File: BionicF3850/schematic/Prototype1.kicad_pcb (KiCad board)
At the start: 2 copper layers, 48.3 x 71.1 mm, 11 parts, among them J1 BionicConnector, U1 F3850, U2 74HCT126, U3 LM78L12

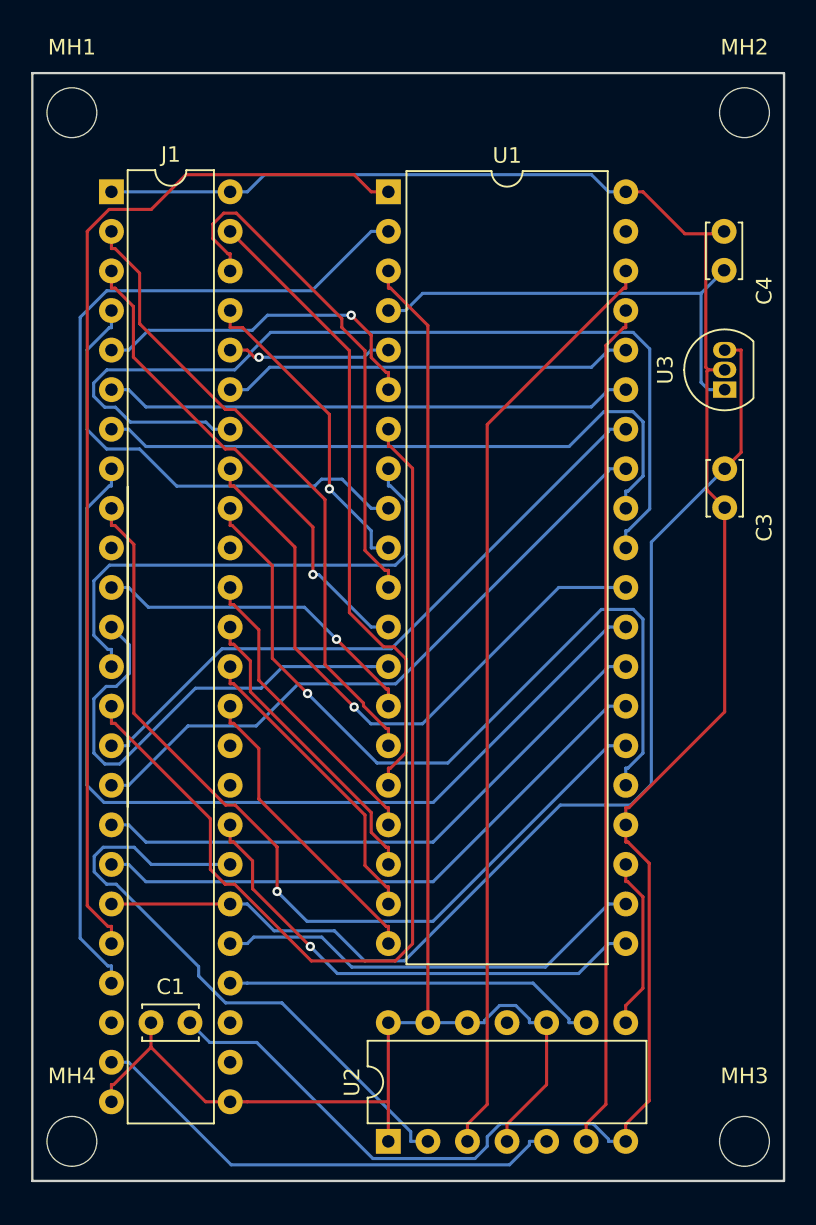
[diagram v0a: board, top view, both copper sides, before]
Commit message: [BionicBase] Add ID EEPROM and change SW and LED conections
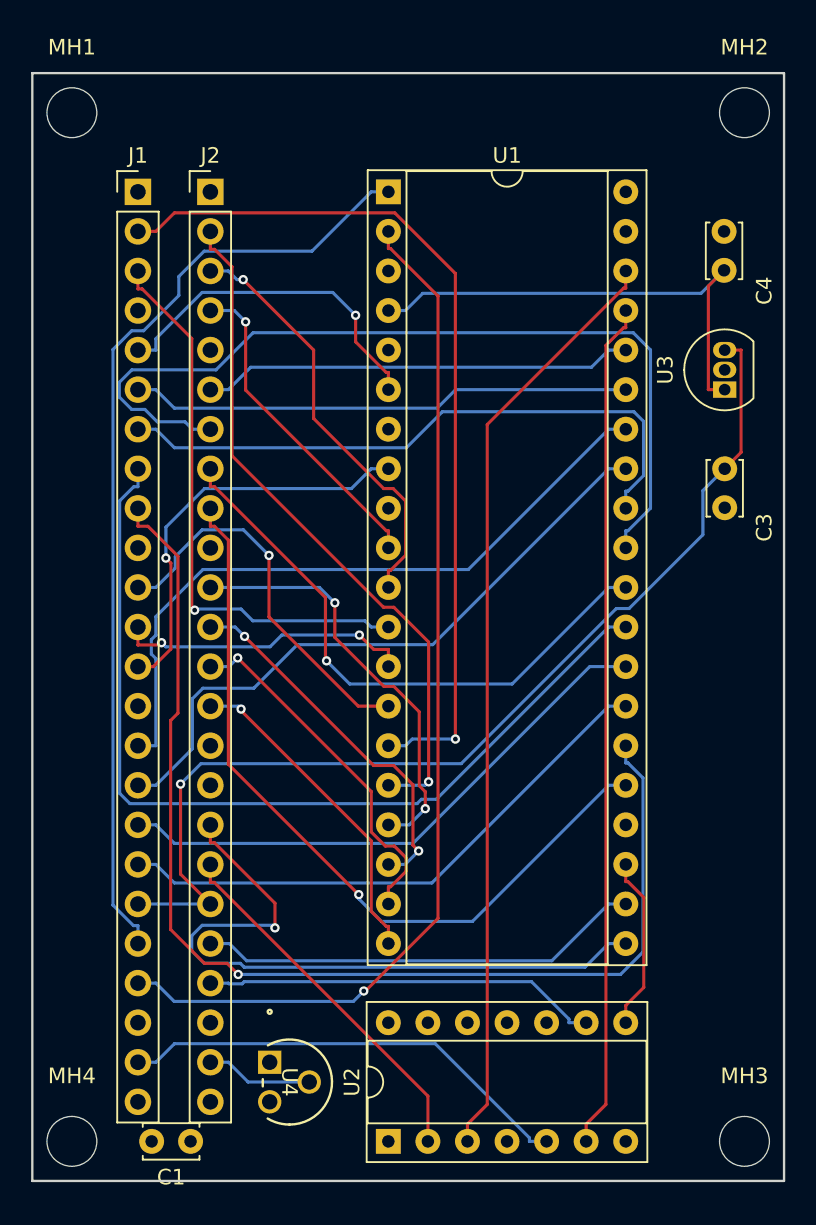
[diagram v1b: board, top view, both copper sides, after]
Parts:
- added J2: Bionic-P245, connector:Bionic-P245_Vertical, F.Cu at (109.9, 75.1)
- added U4: 11AA010-I/TO, 0-LocalLibrary:TO-92_MC_MCH, F.Cu at (113.7, 131.0)
- J1: value BionicConnector -> Bionic-P135; footprint 0-LocalLibrary:DIP-48_W7.62mm -> connector:Bionic-P135_Vertical
- U1: footprint Package_DIP:DIP-40_W15.24mm -> Package_DIP:DIP-40_W15.24mm_Socket
- U2: footprint Package_DIP:DIP-14_W7.62mm -> Package_DIP:DIP-14_W7.62mm_Socket
- moved C1 8.03 mm to (108.6, 136.0), turned to 180 degrees
- moved J1 1.70 mm to (105.2, 75.1)
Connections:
- U2 pad 12: VCC -> GND
- U2 pad 13: VCC -> GND
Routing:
- net GND: track 138.8 -> 0.00 mm
- net VCC: track 99.9 -> 0.00 mm
- net /P33: track 62.9 -> 0.00 mm
- net /P12: track 30.2 -> 0.00 mm
- net /P17: track 57.4 -> 74.6 mm
- net /P47: track 39.7 -> 23.7 mm
- net /P10: track 41.0 -> 56.9 mm, vias 0 -> 1
- net /P31: track 31.7 -> 19.2 mm, vias 0 -> 2
- net /P46: track 31.8 -> 44.1 mm
- net /P23: track 10.5 -> 0.00 mm, vias 1 -> 0
- net /P40: track 19.7 -> 27.2 mm, vias 0 -> 2
- net Net-(J2-P57): track 0.00 -> 6.88 mm
- net /P32: track 32.9 -> 26.4 mm, vias 0 -> 1
- net /P21: track 33.6 -> 27.3 mm, vias 0 -> 1
- net /P50: track 67.8 -> 61.6 mm
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- added copper zone on F.Cu, net GND
- added copper zone on B.Cu, net VCC
